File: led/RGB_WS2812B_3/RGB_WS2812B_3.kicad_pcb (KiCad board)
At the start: 2 copper layers, 3 parts

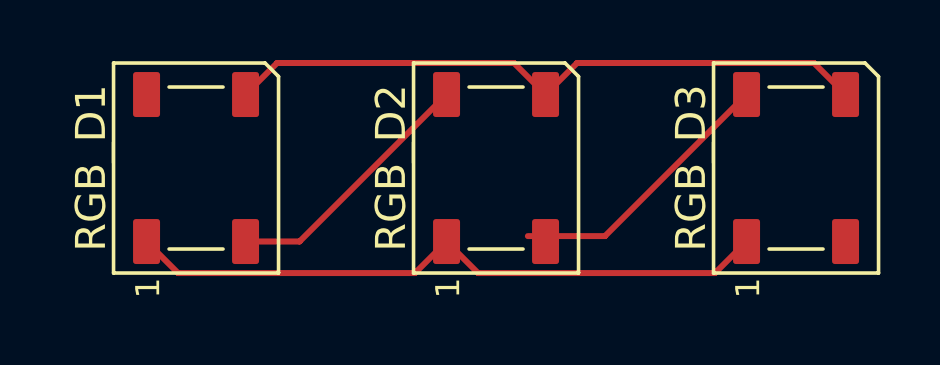
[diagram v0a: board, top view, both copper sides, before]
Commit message: update RGB position
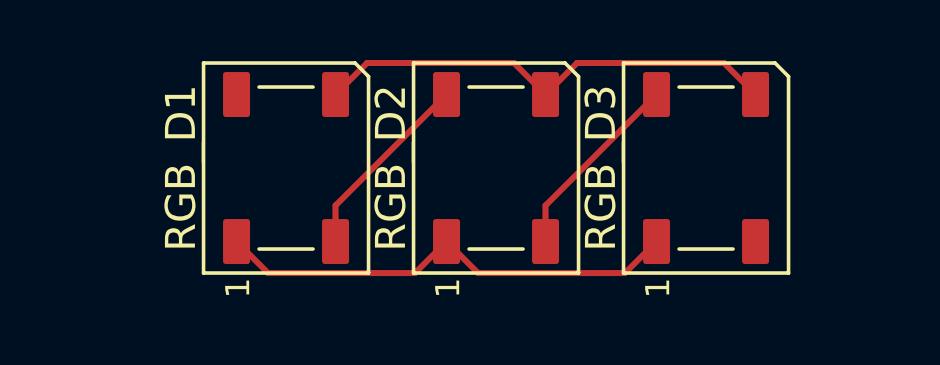
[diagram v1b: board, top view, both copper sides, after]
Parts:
- moved RGB_D1 3.00 mm to (-7.00, 0.00)
- moved RGB_D3 3.00 mm to (7.00, 0.00)
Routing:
- net VIN: track 21.7 -> 15.7 mm
- net GND: track 21.7 -> 15.7 mm
- net Net-(RGB_D2-DOUT): track 9.25 -> 6.43 mm
- net Net-(RGB_D1-DOUT): track 8.73 -> 6.43 mm
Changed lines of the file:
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@@
 	(footprint "ErgoCai.pretty:LED_WS2812B_PLCC4_5.0x5.0mm_P3.2mm"
 		(layer "F.Cu")
-		(at 10 0 90)
+		(at 7 0 90)
 		(descr "5.0mm x 5.0mm Addressable RGB LED NeoPixel, https://cdn-shop.adafruit.com/datasheets/WS2812B.pdf")
 		(tags "LED RGB NeoPixel PLCC-4 5050")
@@
 		)
 		(property "Value" "WS2812B"
-			(at 0 4 90)
+			(at 4.33 0.04 180)
 			(layer "F.Fab")
 			(effects
@@
 		)
 		(property "Value" "WS2812B"
-			(at 0 4 90)
+			(at 4.44 0.01 180)
 			(layer "F.Fab")
 			(effects
@@
 	(footprint "ErgoCai.pretty:LED_WS2812B_PLCC4_5.0x5.0mm_P3.2mm"
 		(layer "F.Cu")
-		(at -10 0 90)
+		(at -7 0 90)
 		(descr "5.0mm x 5.0mm Addressable RGB LED NeoPixel, https://cdn-shop.adafruit.com/datasheets/WS2812B.pdf")
 		(tags "LED RGB NeoPixel PLCC-4 5050")
@@
 		)
 		(property "Value" "WS2812B"
-			(at 0 4 90)
+			(at 4.55 0 180)
 			(layer "F.Fab")
 			(effects
@@
 	)
 	(segment
-		(start 2.701 -3.501)
-		(end 1.65 -2.45)
-		(width 0.2)
-		(layer "F.Cu")
-		(net 1)
-	)
-	(segment
-		(start 10.599 -3.501)
-		(end 2.701 -3.501)
-		(width 0.2)
-		(layer "F.Cu")
-		(net 1)
-	)
-	(segment
-		(start 11.65 -2.45)
-		(end 10.599 -3.501)
-		(width 0.2)
-		(layer "F.Cu")
-		(net 1)
-	)
-	(segment
-		(start -7.299 -3.501)
-		(end 0.599 -3.501)
+		(start -5.35 -2.45)
+		(end -4.299 -3.501)
 		(width 0.2)
 		(layer "F.Cu")
@@
 	)
 	(segment
-		(start -8.35 -2.45)
-		(end -7.299 -3.501)
+		(start -4.299 -3.501)
+		(end 0.599 -3.501)
 		(width 0.2)
 		(layer "F.Cu")
@@
 	)
 	(segment
-		(start -11.65 2.45)
-		(end -10.599 3.501)
+		(start 7.599 -3.501)
+		(end 8.65 -2.45)
+		(width 0.2)
+		(layer "F.Cu")
+		(net 1)
+	)
+	(segment
+		(start 1.65 -2.45)
+		(end 2.701 -3.501)
+		(width 0.2)
+		(layer "F.Cu")
+		(net 1)
+	)
+	(segment
+		(start 2.701 -3.501)
+		(end 7.599 -3.501)
+		(width 0.2)
+		(layer "F.Cu")
+		(net 1)
+	)
+	(segment
+		(start 4.299 3.501)
+		(end -0.599 3.501)
 		(width 0.2)
 		(layer "F.Cu")
@@
 	(segment
 		(start -2.701 3.501)
+		(end -7.599 3.501)
+		(width 0.2)
+		(layer "F.Cu")
+		(net 3)
+	)
+	(segment
+		(start -0.599 3.501)
 		(end -1.65 2.45)
 		(width 0.2)
@@
 	)
 	(segment
-		(start 7.299 3.501)
-		(end 8.35 2.45)
+		(start 5.35 2.45)
+		(end 4.299 3.501)
 		(width 0.2)
 		(layer "F.Cu")
@@
 	)
 	(segment
-		(start -10.599 3.501)
+		(start -1.65 2.45)
 		(end -2.701 3.501)
 		(width 0.2)
@@
 	)
 	(segment
-		(start -0.599 3.501)
-		(end 7.299 3.501)
+		(start -7.599 3.501)
+		(end -8.65 2.45)
 		(width 0.2)
 		(layer "F.Cu")
@@
 	)
 	(segment
-		(start -1.65 2.45)
-		(end -0.599 3.501)
-		(width 0.2)
-		(layer "F.Cu")
-		(net 3)
-	)
-	(segment
-		(start -6.55 2.45)
-		(end -8.35 2.45)
+		(start -5.35 2.45)
+		(end -5.35 1.25)
 		(width 0.2)
 		(layer "F.Cu")
@@
 	)
 	(segment
-		(start -1.65 -2.45)
-		(end -6.55 2.45)
+		(start -5.35 1.25)
+		(end -1.65 -2.45)
 		(width 0.2)
 		(layer "F.Cu")
@@
 	)
 	(segment
-		(start 3.63 2.27)
-		(end 1.06 2.27)
+		(start 1.65 1.25)
+		(end 5.35 -2.45)
 		(width 0.2)
 		(layer "F.Cu")
@@
 	)
 	(segment
-		(start 8.35 -2.45)
-		(end 3.63 2.27)
-		(width 0.2)
-		(layer "F.Cu")
+		(start 1.65 2.45)
+		(end 1.65 1.25)
+		(width 0.2)
+		(layer "F.Cu")

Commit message: update RGB LEB pin name
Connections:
- net DIN renamed GPIO_DIN
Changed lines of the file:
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@@
 	(net 0 "")
 	(net 1 "GND")
-	(net 2 "DIN")
+	(net 2 "GPIO_DIN")
 	(net 3 "VIN")
 	(net 4 "Net-(RGB_D1-DOUT)")
@@
 			(layers "F.Cu" "F.Mask" "F.Paste")
 			(roundrect_rratio 0.1)
-			(net 2 "DIN")
+			(net 2 "GPIO_DIN")
 			(pinfunction "DIN")
 			(pintype "input")

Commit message: use vcc instead of vin in led
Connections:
- net VIN renamed VCC
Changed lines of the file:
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@@
 	(net 1 "GND")
 	(net 2 "GPIO_DIN")
-	(net 3 "VIN")
+	(net 3 "VCC")
 	(net 4 "Net-(RGB_D1-DOUT)")
 	(net 5 "Net-(RGB_D2-DOUT)")
@@
 			(layers "F.Cu" "F.Mask" "F.Paste")
 			(roundrect_rratio 0.1)
-			(net 3 "VIN")
+			(net 3 "VCC")
 			(pinfunction "VDD")
 			(pintype "power_in")
@@
 			(layers "F.Cu" "F.Mask" "F.Paste")
 			(roundrect_rratio 0.1)
-			(net 3 "VIN")
+			(net 3 "VCC")
 			(pinfunction "VDD")
 			(pintype "power_in")
@@
 			(layers "F.Cu" "F.Mask" "F.Paste")
 			(roundrect_rratio 0.1)
-			(net 3 "VIN")
+			(net 3 "VCC")
 			(pinfunction "VDD")
 			(pintype "power_in")

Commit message: update to 3.3V tag
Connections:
- net VCC renamed 3.3V
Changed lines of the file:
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@@
 	(net 1 "GND")
 	(net 2 "GPIO_DIN")
-	(net 3 "VCC")
+	(net 3 "3.3V")
 	(net 4 "Net-(RGB_D1-DOUT)")
 	(net 5 "Net-(RGB_D2-DOUT)")
@@
 			(layers "F.Cu" "F.Mask" "F.Paste")
 			(roundrect_rratio 0.1)
-			(net 3 "VCC")
+			(net 3 "3.3V")
 			(pinfunction "VDD")
 			(pintype "power_in")
@@
 			(layers "F.Cu" "F.Mask" "F.Paste")
 			(roundrect_rratio 0.1)
-			(net 3 "VCC")
+			(net 3 "3.3V")
 			(pinfunction "VDD")
 			(pintype "power_in")
@@
 			(layers "F.Cu" "F.Mask" "F.Paste")
 			(roundrect_rratio 0.1)
-			(net 3 "VCC")
+			(net 3 "3.3V")
 			(pinfunction "VDD")
 			(pintype "power_in")
